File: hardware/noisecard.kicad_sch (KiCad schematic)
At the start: 32 parts, among them J1 Conn_ARM_SWD_TagConnect_TC203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, SW1 SW_DPDT_x2, U1 STM32G031F6Px, U2 LM3670MF

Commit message: schematic cleanup
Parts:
- C1: value 4u7 -> 4.7uF
- C2: value 10u -> 10uF
- C3, C4: value 330u -> 330uF
- C5, C6, C9: value 0.1U -> 0.1uF
- C7: value 200P -> 200pF
- C8: value 2U2 -> 2.2uF
- L1: value 10u -> 10uH
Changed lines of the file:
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@@
       (effects (font (size 1.27 1.27)) (justify left))
     )
-    (property "Value" "330u" (at 73.66 35.306 0)
+    (property "Value" "330uF" (at 73.66 35.306 0)
       (effects (font (size 1.27 1.27)) (justify left))
     )
@@
       (effects (font (size 1.27 1.27)) (justify right))
     )
-    (property "Value" "2U2" (at 50.165 117.4813 0)
+    (property "Value" "2.2uF" (at 50.165 117.4813 0)
       (effects (font (size 1.27 1.27)) (justify right))
     )
@@
       (effects (font (size 1.27 1.27)) (justify right))
     )
-    (property "Value" "0.1U" (at 61.595 117.4813 0)
+    (property "Value" "0.1uF" (at 61.595 117.4813 0)
       (effects (font (size 1.27 1.27)) (justify right))
     )
@@
       (effects (font (size 1.27 1.27)) (justify left))
     )
-    (property "Value" "4u7" (at 102.87 36.195 0)
+    (property "Value" "4.7uF" (at 102.87 36.195 0)
       (effects (font (size 1.27 1.27)) (justify left))
     )
@@
       (effects (font (size 1.27 1.27)) (justify left))
     )
-    (property "Value" "10u" (at 148.59 36.195 0)
+    (property "Value" "10uF" (at 148.59 36.195 0)
       (effects (font (size 1.27 1.27)) (justify left))
     )
@@
       (effects (font (size 1.27 1.27)) (justify left))
     )
-    (property "Value" "330u" (at 88.9 35.306 0)
+    (property "Value" "330uF" (at 88.9 35.306 0)
       (effects (font (size 1.27 1.27)) (justify left))
     )
@@
       (effects (font (size 1.27 1.27)))
     )
-    (property "Value" "10u" (at 135.255 27.305 90)
+    (property "Value" "10uH" (at 135.255 27.305 90)
       (effects (font (size 1.27 1.27)))
     )
@@
       (effects (font (size 1.27 1.27)) (justify right))
     )
-    (property "Value" "0.1U" (at 245.11 41.2813 0)
+    (property "Value" "0.1uF" (at 245.11 41.2813 0)
       (effects (font (size 1.27 1.27)) (justify right))
     )
@@
       (effects (font (size 1.27 1.27)) (justify right))
     )
-    (property "Value" "0.1U" (at 66.675 92.7163 0)
+    (property "Value" "0.1uF" (at 66.675 92.7163 0)
       (effects (font (size 1.27 1.27)) (justify right))
     )
@@
       (effects (font (size 1.27 1.27)) (justify right))
     )
-    (property "Value" "200P" (at 254 41.2813 0)
+    (property "Value" "200pF" (at 254 41.2813 0)
       (effects (font (size 1.27 1.27)) (justify right))
     )

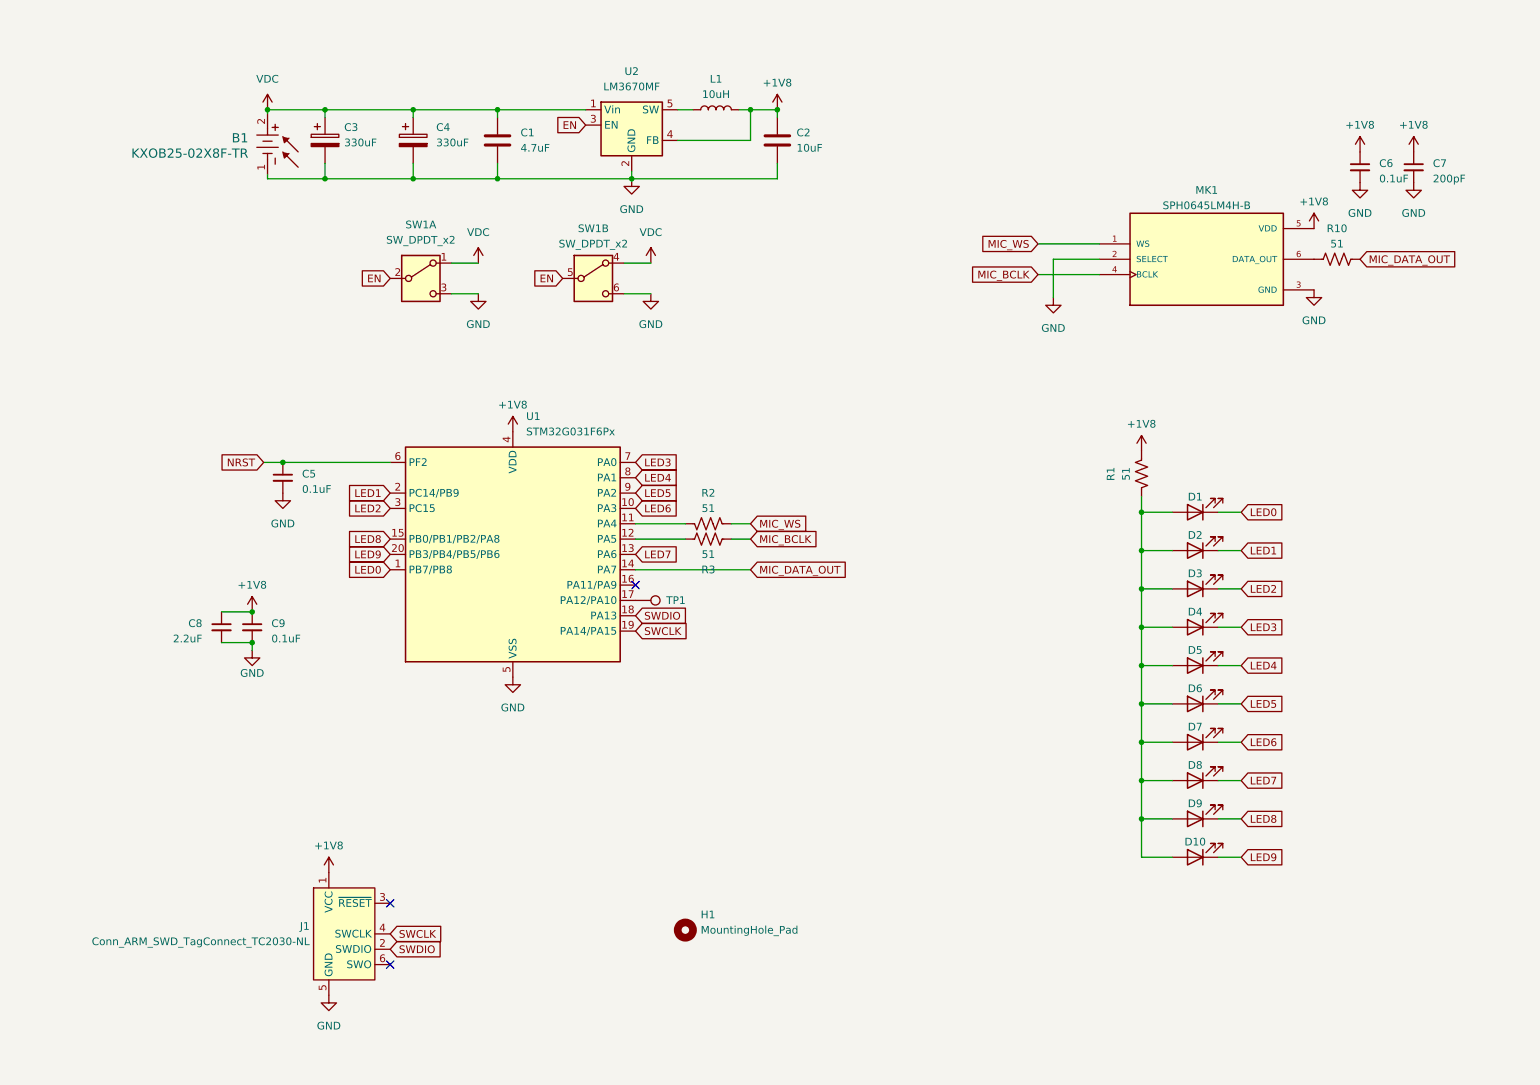
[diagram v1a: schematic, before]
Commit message: add energy harvester and supercaps
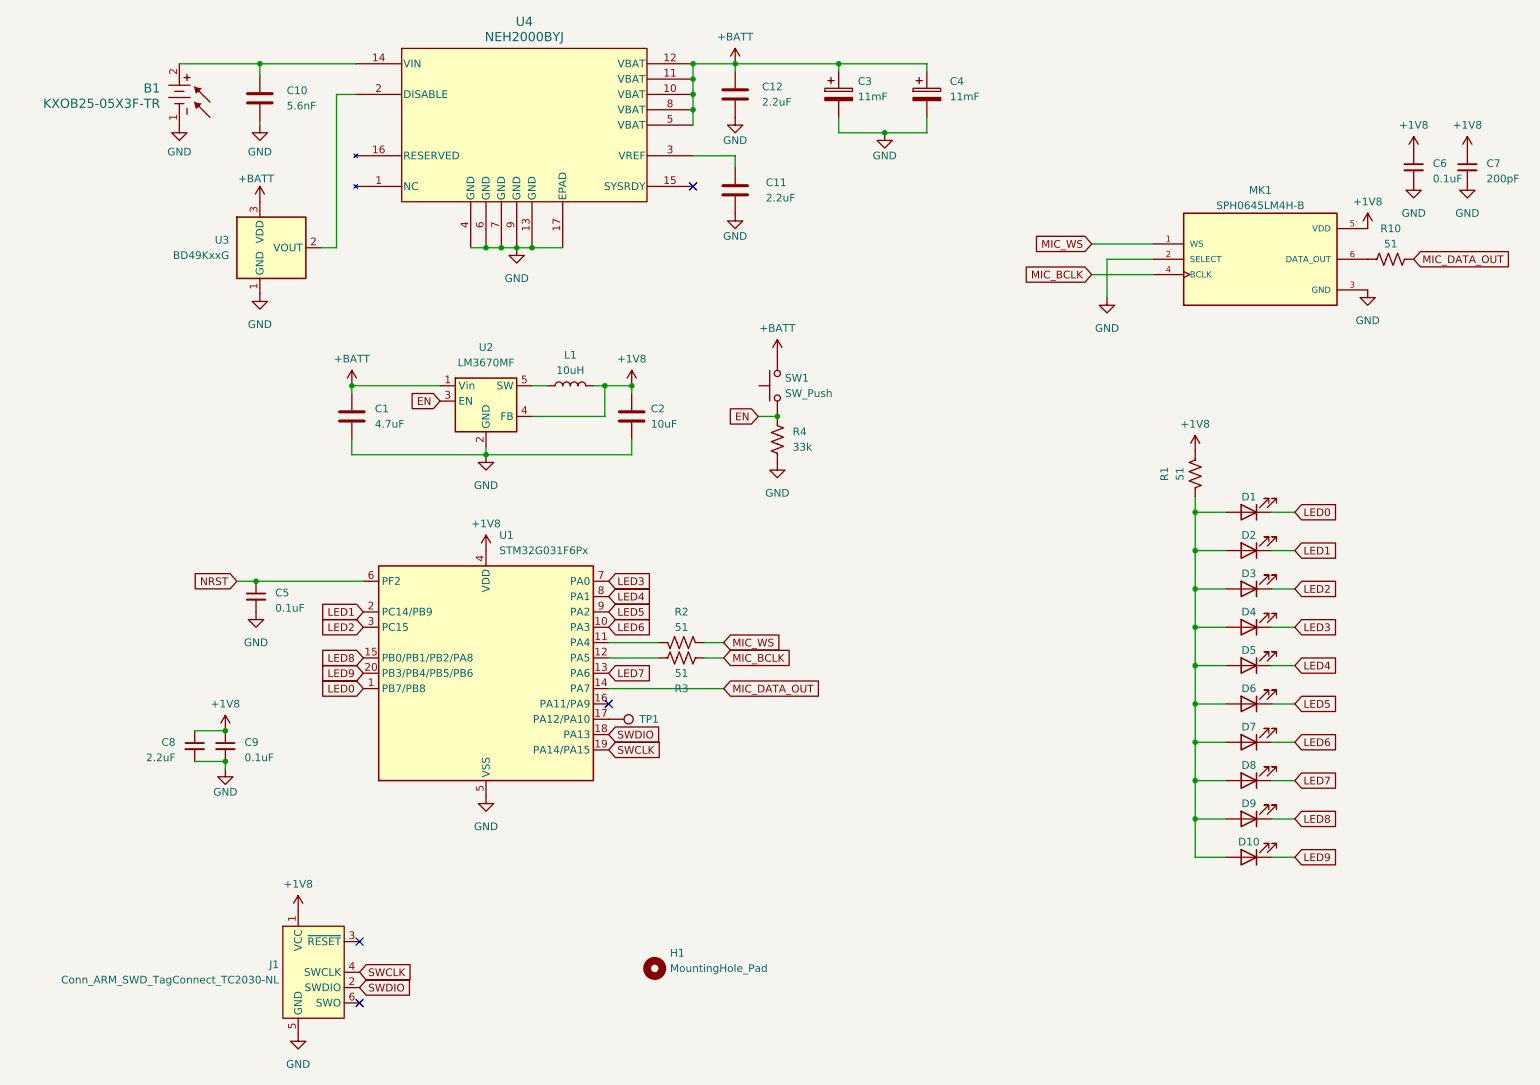
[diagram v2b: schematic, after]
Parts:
- removed SW1: SW_DPDT_x2, Button_Switch_SMD:SW_DPDT_CK_JS202011JCQN, symbol Switch:SW_DPDT_x2
- added C10: 5.6nF, Capacitor_SMD:C_0603_1608Metric, symbol Device:C
- added C11, C12: 2.2uF, Capacitor_SMD:C_0805_2012Metric, symbol Device:C
- added R4: 33k, Resistor_SMD:R_0603_1608Metric, symbol Device:R_US
- added SW1: SW_Push, Button_Switch_SMD:SW_SPST_EVQP0, symbol Switch:SW_Push
- added U3: BD49KxxG, Package_TO_SOT_SMD:SOT-23, symbol Power_Management:BD49KxxG
- added U4: NEH2000BYJ, footprints:HWQFN16_SOT8076-1_NEX, symbol 2024-06-10_19-49-35:NEH2000BYJ
- B1: value KXOB25-02X8F-TR -> KXOB25-05X3F-TR; Part Number KXOB25-02X8F-TR -> KXOB25-05X3F-TR
- C3, C4: value 330uF -> 11mF; footprint Capacitor_Tantalum_SMD:CP_EIA-7343-15_Kemet-W -> Capacitor_SMD:C_1210_3225Metric; Part Number 6TPE330MAP -> CPH3225A
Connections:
- net EN: now also R4.2, SW1.1
- net GND: now also C10.2, C11.2, C12.2, R4.1, U3.1 (GND), U4.13 (GND), U4.17 (EPAD), U4.4 (GND), U4.6 (GND), U4.7 (GND), U4.9 (GND)
- net VDC renamed +BATT
- net +BATT: now also C12.1, SW1.2, U3.3 (VDD), U4.10 (VBAT), U4.11 (VBAT), U4.12 (VBAT), U4.5 (VBAT), U4.8 (VBAT); no longer B1.2
- new net: B1.2, C10.1, U4.14 (VIN)
- new net: C11.1, U4.3 (VREF)
- new net: U3.2 (VOUT), U4.2 (DISABLE)
- no-connect marks 3 -> 4
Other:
- moved on the sheet: B1, C1, C2, C3, C4, C5, C6, C7, C8, C9, D1, D10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

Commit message: finish up rev2 design
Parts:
- removed H1: MountingHole_Pad, MountingHole:MountingHole_2.5mm, symbol Mechanical:MountingHole
- removed J1: Conn_ARM_SWD_TagConnect_TC2030-NL, Connector:Tag-Connect_TC2030-IDC-NL_2x03_P1.27mm_Vertical, symbol Connector:Conn_ARM_SWD_TagConnect_TC2030-NL
- removed TP1: TestPoint, TestPoint:TestPoint_Pad_D1.0mm, symbol Connector:TestPoint
- added J2: Conn_02x07_Odd_Even, Connector_PinHeader_2.54mm:PinHeader_2x07_P2.54mm_Vertical, symbol Connector_Generic:Conn_02x07_Odd_Even
- added TP2, TP3: TestPoint, TestPoint:TestPoint_THTPad_3.0x3.0mm_Drill1.5mm, symbol Connector:TestPoint
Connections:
- net +1V8: now also J2.14 (Pin_14)
- net GND: now also J2.2 (Pin_2), TP3.1
- net LED0: now also J2.1 (Pin_1)
- net LED1: now also J2.4 (Pin_4)
- net LED2: now also J2.3 (Pin_3)
- net LED3: now also J2.6 (Pin_6)
- net LED4: now also J2.5 (Pin_5)
- net LED5: now also J2.8 (Pin_8)
- net LED6: now also J2.7 (Pin_7)
- net LED7: now also J2.10 (Pin_10)
- net LED8: now also J2.9 (Pin_9)
- net LED9: now also J2.12 (Pin_12)
- net SWCLK: now also J2.11 (Pin_11)
- net SWDIO: now also J2.13 (Pin_13)
- net at B1.2, C10.1, U4.14 (VIN): now also TP2.1
- no-connect marks 4 -> 3
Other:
- moved on the sheet: C5, C8, C9, D1, D10, D2, D3, D4, D5, D6, D7, D8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
